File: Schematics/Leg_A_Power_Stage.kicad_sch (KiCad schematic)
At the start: 38 parts, among them Q3 C3M0025065K, Q7 C3M0025065K, U1 UCC21710QDWRQ1, U2 UCC21710QDWRQ1

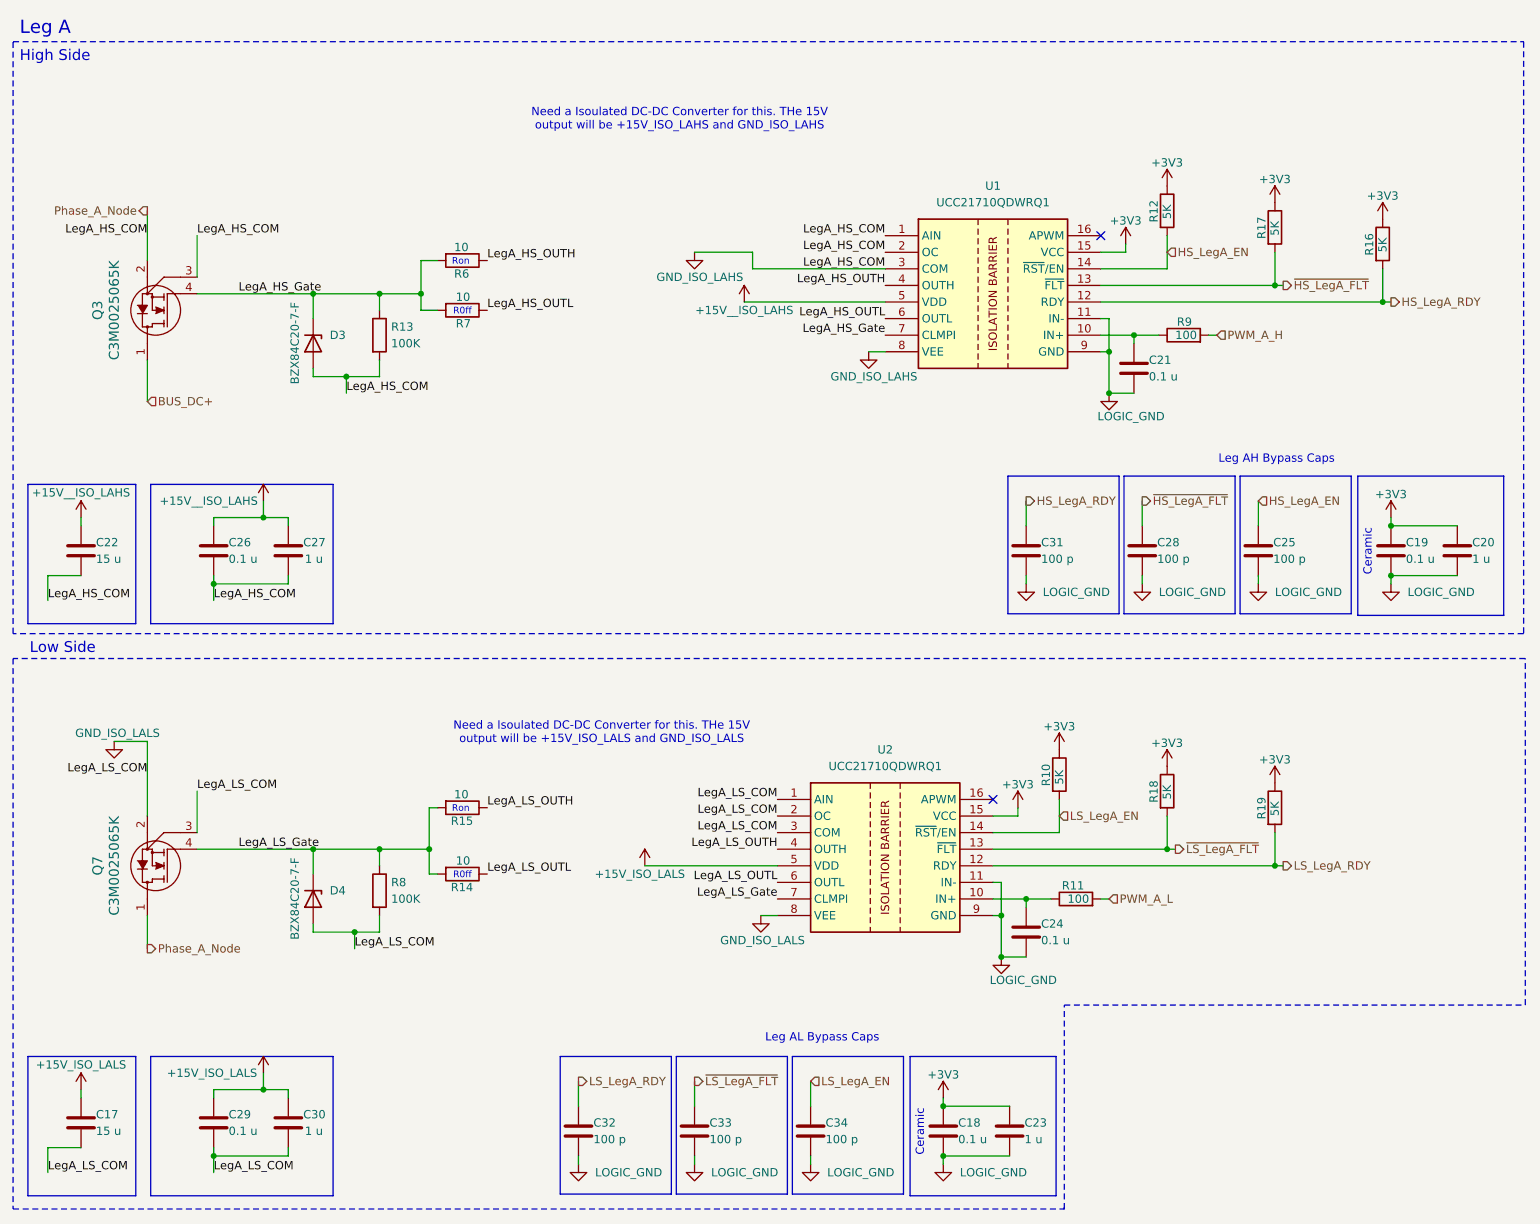
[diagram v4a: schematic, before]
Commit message: [WIP Single Phase SiC Inverter]
- Added molex 4 pin pcb connector for +15V power
- Added 3d model, symbol and footprint
- Added datasheet for molex connector
- Added Male and Female pcb - pcb connectors to all sub sheets
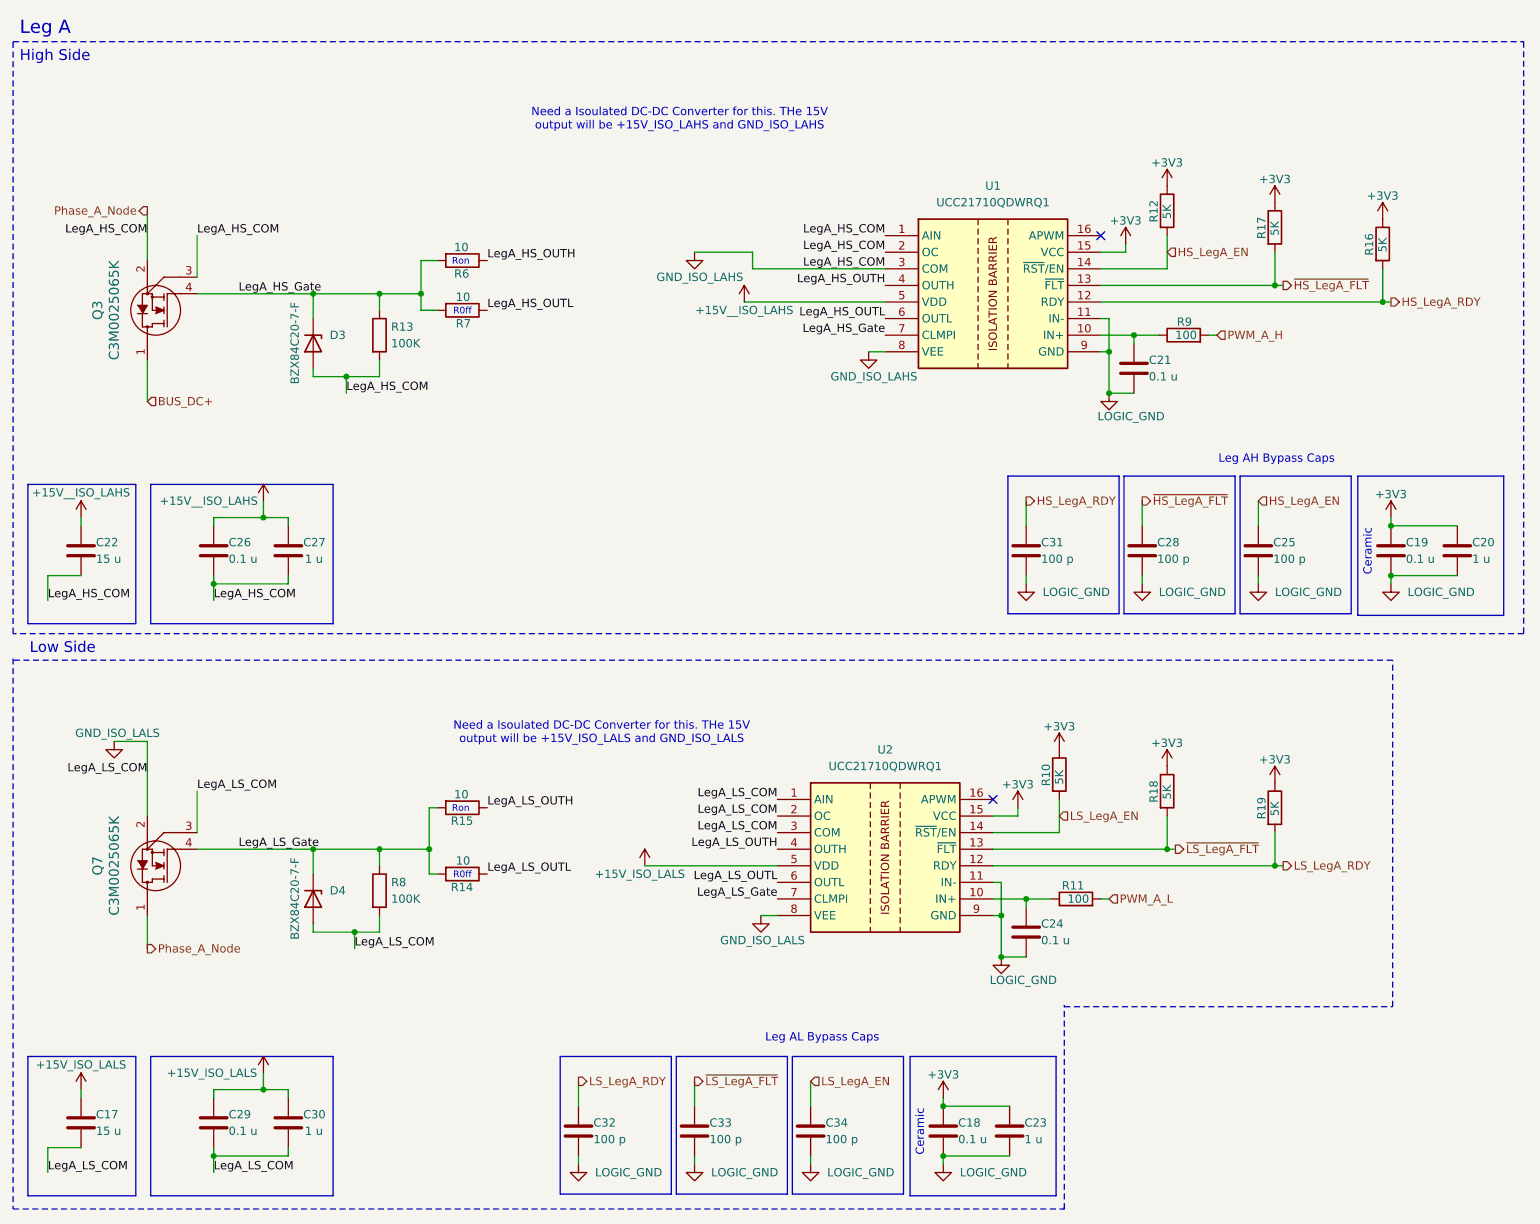
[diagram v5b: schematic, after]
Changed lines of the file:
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@@
 	(polyline
 		(pts
-			(xy 176.022 164.846) (xy 246.634 164.846)
+			(xy 176.022 165.1) (xy 226.314 165.1)
 		)
 		(stroke
@@
 	(polyline
 		(pts
-			(xy 246.634 164.846) (xy 246.634 111.76)
+			(xy 226.314 165.1) (xy 226.314 112.014)
 		)
 		(stroke
@@
 	(polyline
 		(pts
-			(xy 246.634 111.76) (xy 14.986 111.76)
-		)
-		(stroke
+			(xy 226.314 112.014) (xy 14.986 112.014)
+		)
+		(stroke

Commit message: [WIP Single Phase Inverter]
- Changed all Refs within each sub sheet (Stripe)
- Added 3V3 Power Supply off of 15V iso supply
- Added footprint, symbol and 3d part
- updated PCB with new part
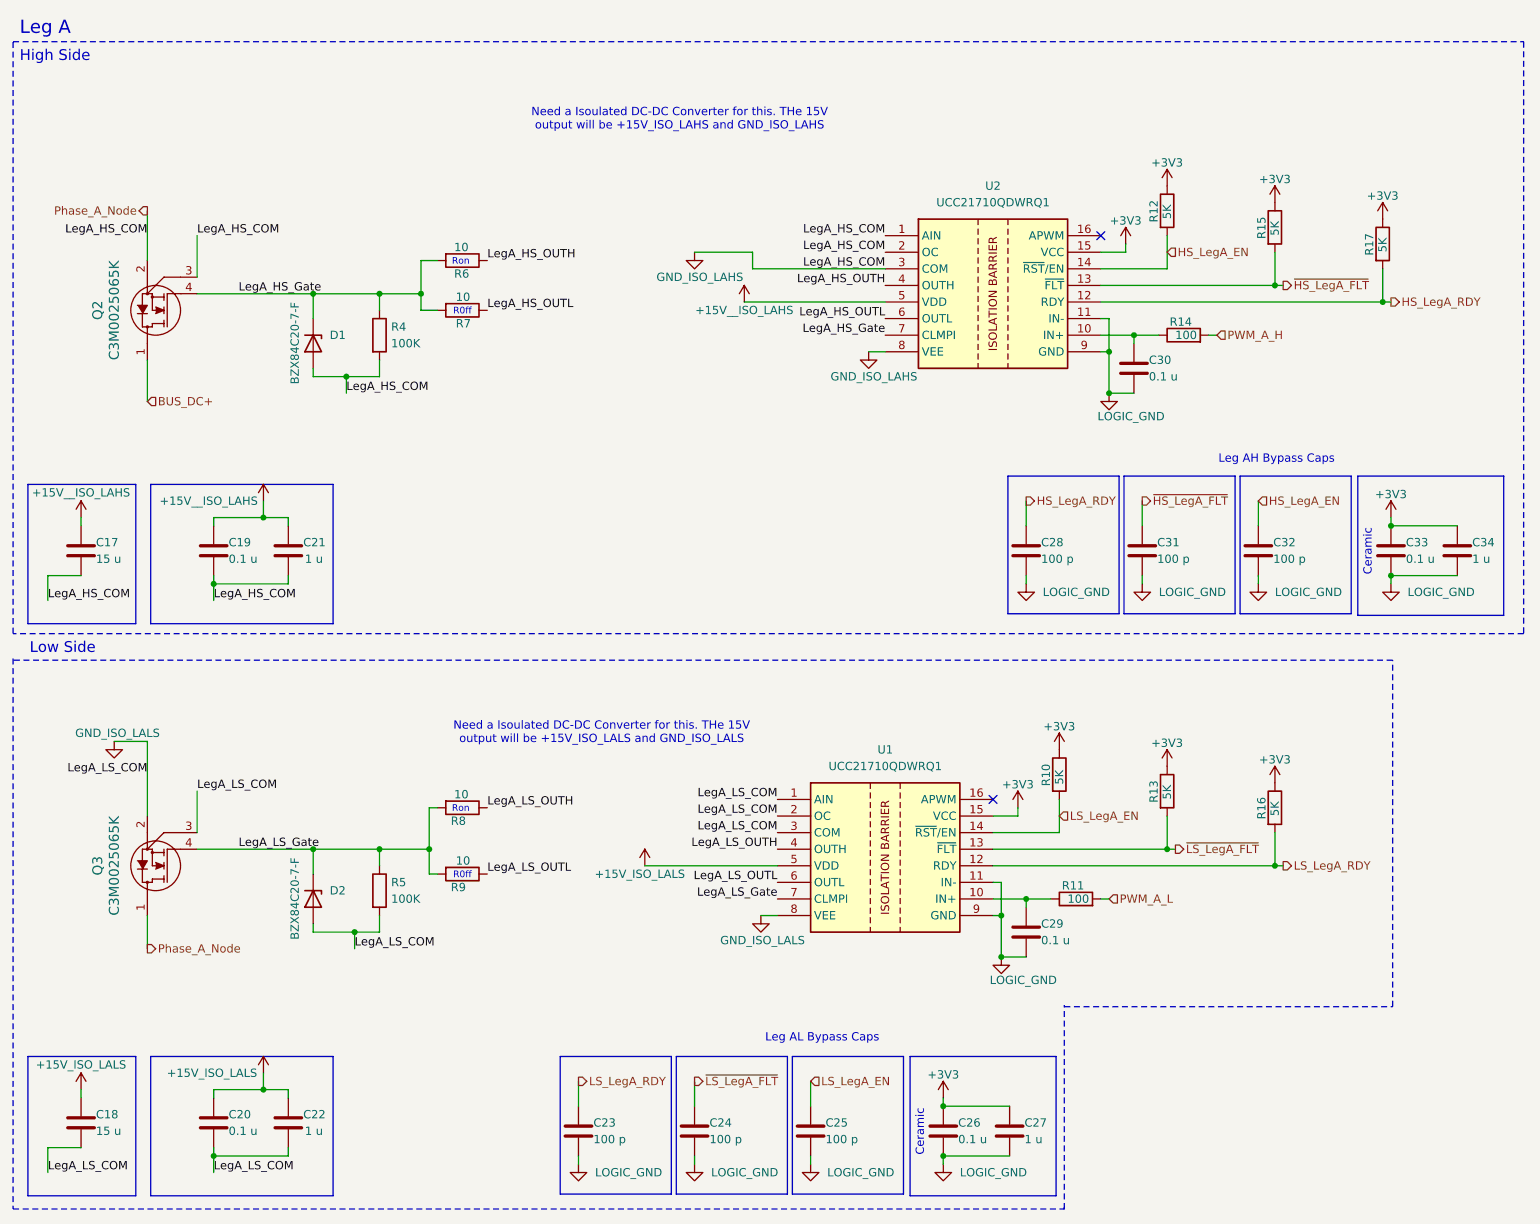
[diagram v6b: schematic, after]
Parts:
- renumbered C22 to C17, C17 to C18, C26 to C19, C29 to C20, C27 to C21, C30 to C22, C32 to C23, C33 to C24, C34 to C25, C18 to C26, C23 to C27, C31 to C28, C24 to C29, C21 to C30, C28 to C31, C25 to C32, C19 to C33, C20 to C34, D3 to D1, D4 to D2, Q3 to Q2, Q7 to Q3, R18 to R13, R9 to R14, R17 to R15, R19 to R16, R16 to R17, R13 to R4, R8 to R5, R15 to R8, R14 to R9, U2 to U1, U1 to U2

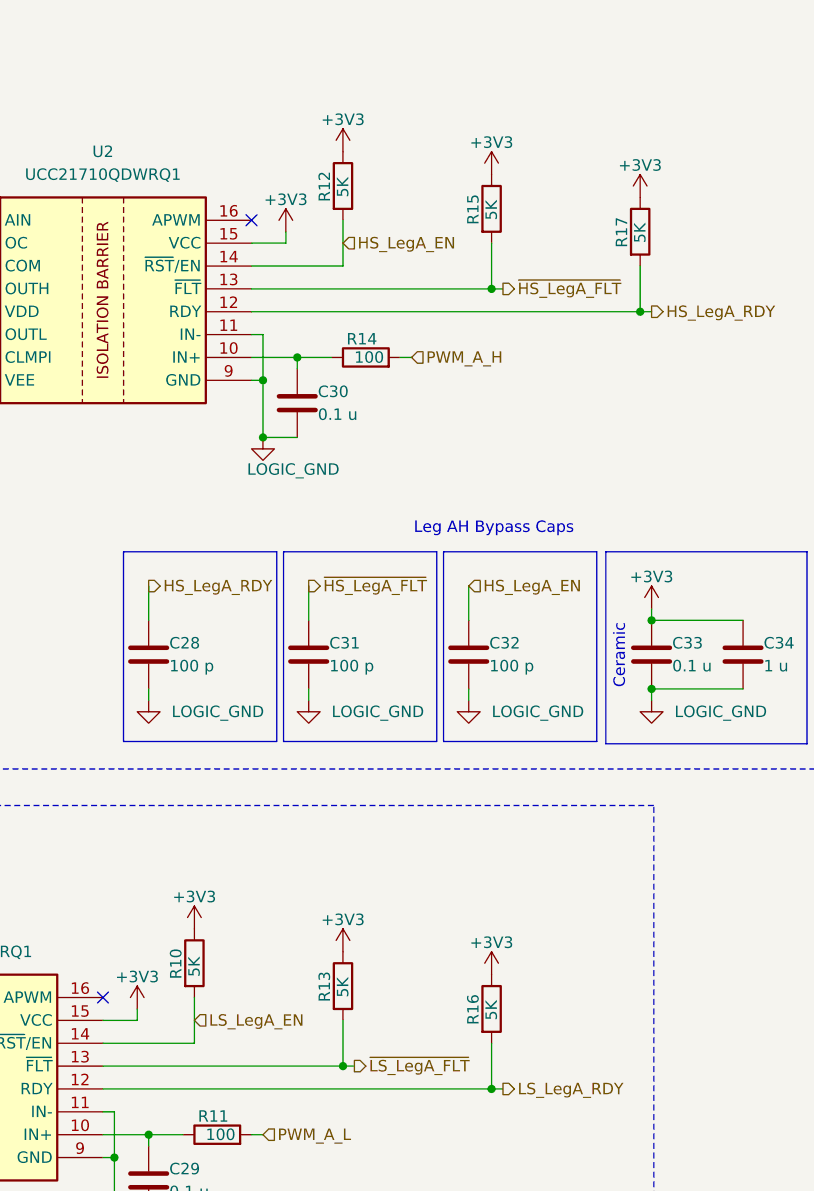
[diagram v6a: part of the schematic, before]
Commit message: WIP: Work on Controller layout, and fixed some sheet text and positions
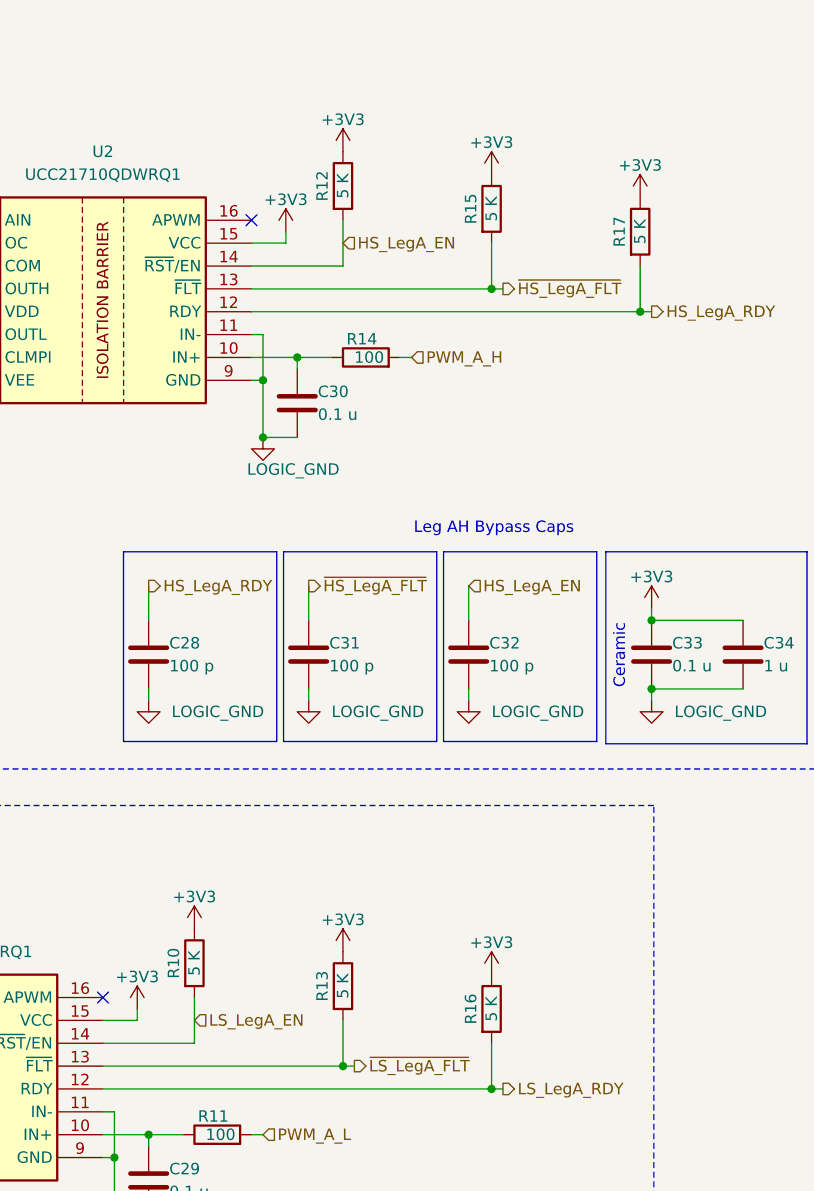
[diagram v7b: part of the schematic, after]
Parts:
- R10, R12, R13, R15, R16, R17: value 5K -> 5 K; symbol Device:R -> SiC_Inverter:RT1206BRD075KL
